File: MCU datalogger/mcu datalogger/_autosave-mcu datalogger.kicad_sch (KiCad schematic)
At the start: 25 parts, among them U1 24LC1025, U2 DS1337S_, U3 24LC1025, U4 ATMEGA328P-AU, Y1 32.768 KHz, Y2 16MHz

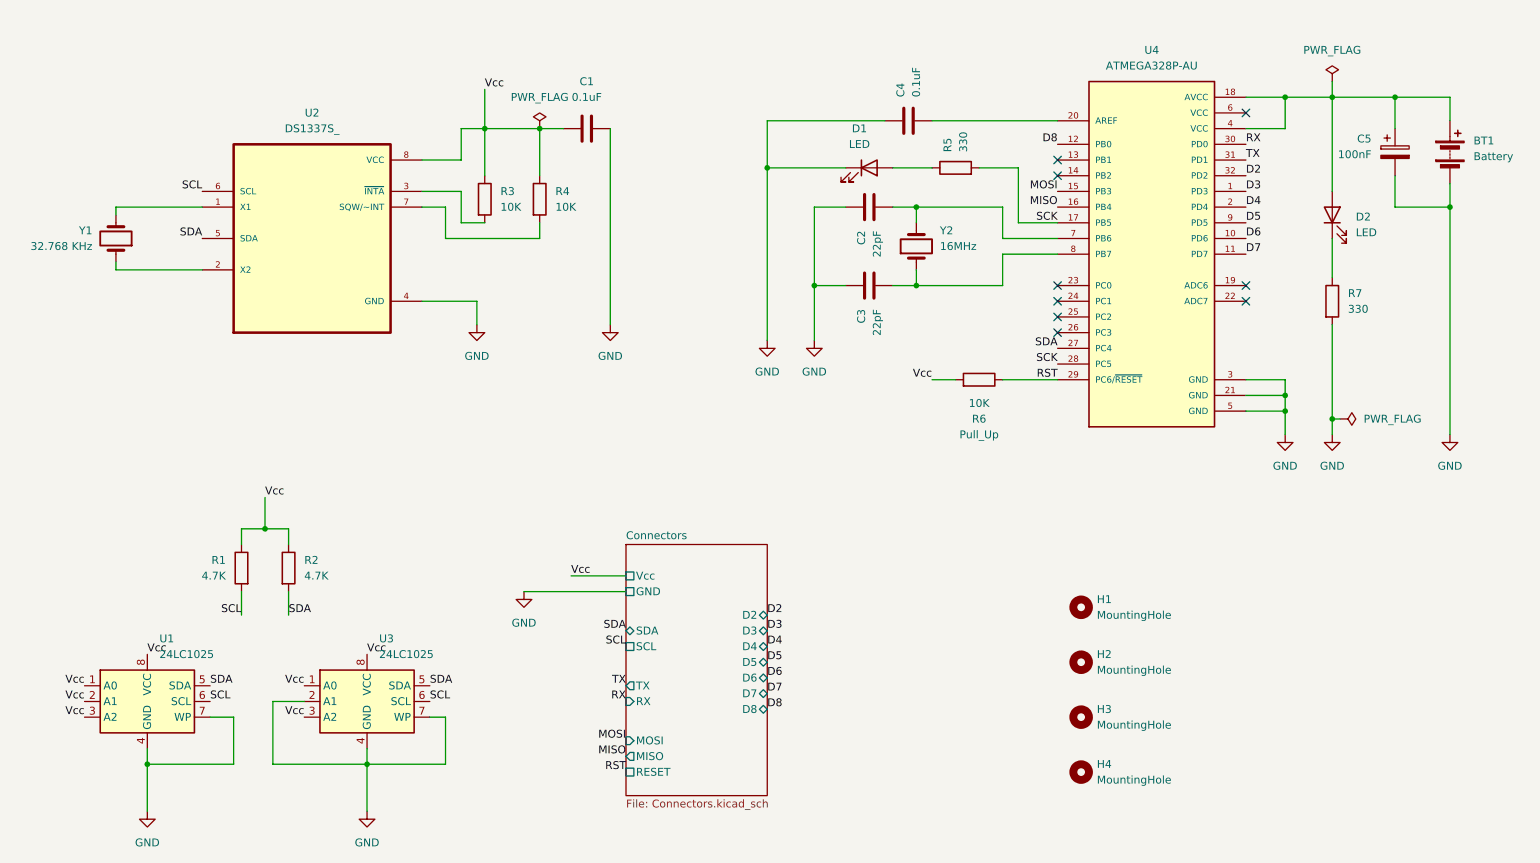
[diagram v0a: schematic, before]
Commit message: Setup PCBnew.
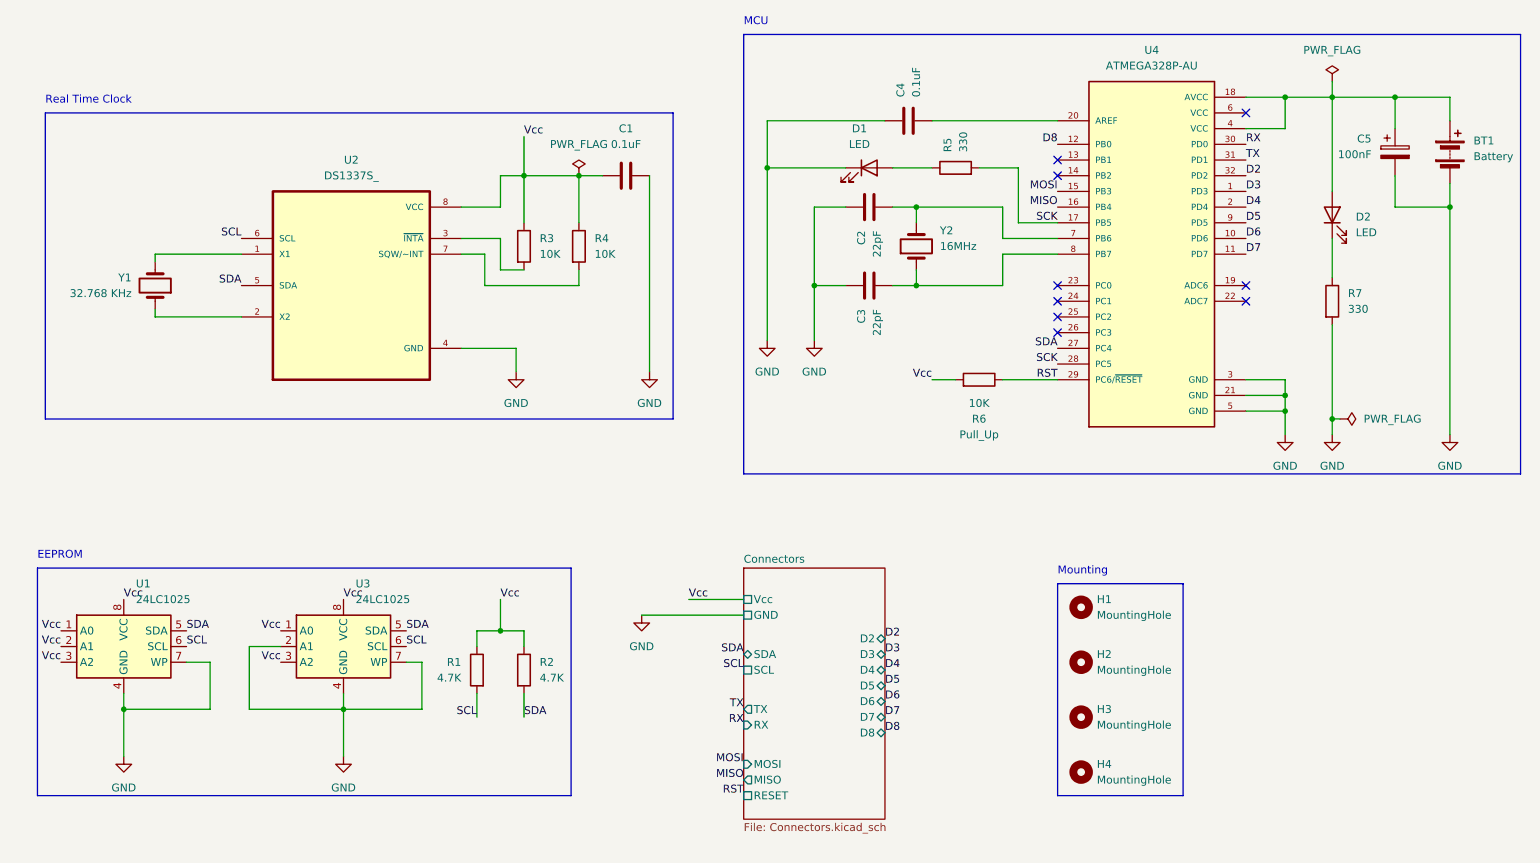
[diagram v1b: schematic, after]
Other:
- note added: "EEPROM"
- note added: "MCU"
- note added: "Mounting"
- note added: "Real Time Clock"
- moved on the sheet: C1, R1, R2, R3, R4, U1, U2, U3, Y1
